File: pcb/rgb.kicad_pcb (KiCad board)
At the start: 2 copper layers, 58 x 48 mm, 59 parts, among them J1 2.54-2*8P, J3 B4PS-VH, J4 TYPE-C-31-M-12, J5 TF-01A, J7 B4PS-VH, U1 SY8286ARAC, U2 SY8286ARAC, U4 TACTILE, U5 ESP32-WROOM-32E, U7 CH340C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

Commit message: do we have space fo the RTC?
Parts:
- added BT1: CR2032, Battery:BatteryHolder_Multicomp_BC-2001_1x2032, B.Cu at (56.0, 98.0)
- added C30: 2u2, Capacitor_SMD:C_0603_1608Metric, F.Cu at (65.5, 118.5)
- added R12: 10k, Resistor_SMD:R_0603_1608Metric, F.Cu at (80.5, 113.5)
- added R14: 1k, Resistor_SMD:R_0603_1608Metric, F.Cu at (64.0, 102.5)
- added R16: 10k, Resistor_SMD:R_0603_1608Metric, F.Cu at (70.0, 77.0)
- added R17: 10k, Resistor_SMD:R_0603_1608Metric, F.Cu at (56.8, 105.0)
- added R18: 10k, Resistor_SMD:R_0603_1608Metric, F.Cu at (52.2, 105.0)
- added R19: 10k, Resistor_SMD:R_0603_1608Metric, F.Cu at (50.8, 105.0)
- added R20: 10k, Resistor_SMD:R_0603_1608Metric, F.Cu at (49.2, 105.0)
- added R21: 10k, Resistor_SMD:R_0603_1608Metric, F.Cu at (58.2, 105.0)
- added R22: 1k, Resistor_SMD:R_0603_1608Metric, F.Cu at (78.5, 99.5)
- added R23: 1k, Resistor_SMD:R_0603_1608Metric, F.Cu at (77.5, 97.0)
- added R24: 1k, Resistor_SMD:R_0603_1608Metric, F.Cu at (81.5, 99.5)
- added R25: 10k, Resistor_SMD:R_0603_1608Metric, F.Cu at (67.0, 112.5)
- added R26: 10k, Resistor_SMD:R_0603_1608Metric, F.Cu at (67.0, 114.0)
- added R4: 10k, Resistor_SMD:R_0603_1608Metric, F.Cu at (55.2, 105.0)
- added U3: DS3232M, Package_SO:SOIC-8_3.9x4.9mm_P1.27mm, F.Cu at (69.5, 118.5)
- D2: value GREEN -> GRN
- R10: value 56k -> 24k
- R13: value 22k -> 10k
- R6: value 10k -> 24k
- R7: value 22k -> 19k8
- U4: value TACTILE -> EVQQ2
- moved C6 4.93 mm to (74.0, 114.0), turned to 180 degrees
- moved J5 3.00 mm to (54.0, 113.5)
- moved C4 2.61 mm to (53.8, 105.0), turned to 90 degrees
- moved R14 0.25 mm to (65.5, 102.5)
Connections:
- J5 pad 1: unconnected-(J5-DAT2-Pad1) -> Net-(J5-DAT2)
- J5 pad 2: /SD_CS -> Net-(J5-DAT3/CD)
- J5 pad 3: /SD_MOSI -> /SD_CMD
- J5 pad 7: /SD_MISO -> /SD_D0
- J5 pad 8: unconnected-(J5-DAT1-Pad8) -> /SD_D1
- R9 pad 2: Net-(U5-IO33) -> Net-(U5-IO12)
- U5 pad 10: /SD_MISO -> /STB
- U5 pad 11: /SD_CLK -> /C
- U5 pad 12: /SD_MOSI -> /CLK
- U5 pad 13: /SD_CS -> /SD_CLK
- U5 pad 14: /OE -> Net-(U5-IO12)
- U5 pad 16: /CLK -> Net-(U5-IO13)
- U5 pad 23: /STB -> /SD_CMD
- U5 pad 24: /C -> /SD_D0
- U5 pad 25: Net-(U5-IO0) -> /esp_prog
- U5 pad 26: /D -> /SD_D1
- U5 pad 8: /E -> /D
- U5 pad 9: Net-(U5-IO33) -> /OE
- U7 pad 5: /USB_P -> /USB_P_S
- U7 pad 6: /USB_N -> /USB_N_S
- U9 pad 4: Net-(U9-DM) -> /USB_P_P
- U9 pad 5: Net-(U9-DM) -> /USB_N_P
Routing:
- net Net-(U5-IO33): track 35.3 -> 0.00 mm, vias 4 -> 0
- net /OE: track 35.3 -> 70.6 mm, vias 1 -> 5
- net /C: track 11.8 -> 38.0 mm, vias 1 -> 5
- net /SD_CS: track 24.9 -> 0.00 mm, vias 2 -> 0
- net /STB: track 18.5 -> 31.1 mm
- net /SD_MISO: track 12.7 -> 0.00 mm
- net /SD_CLK: track 26.2 -> 24.9 mm, vias 4 -> 2
- net GND: track 14.8 -> 13.5 mm, vias 81 -> 80
- net /RTC_SCL: track 0.00 -> 1.22 mm, vias 0 -> 1
- net Net-(U9-DM): track 1.00 -> 0.00 mm
- net (no net): track 0.00 -> 1.00 mm
- net /SD_MOSI: vias 4 -> 0
- net /CLK: vias 3 -> 7

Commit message: pcb: started to place components
looks like the Rev: 3 PCB will be the same size as Rev: 2
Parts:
- removed BT1: CR2032, Battery:BatteryHolder_Multicomp_BC-2001_1x2032
- removed C30: 2u2, Capacitor_SMD:C_0603_1608Metric
- removed R12, R13, R26: 10k, Resistor_SMD:R_0603_1608Metric
- removed the R14 at (65.5, 102.5)
- removed the R4 at (45.8, 89.5)
- removed U3: DS3232M, Package_SO:SOIC-8_3.9x4.9mm_P1.27mm
- added C31: 2u2, Capacitor_SMD:C_0603_1608Metric, F.Cu at (45.8, 89.0)
- added C32: 2u2, Capacitor_SMD:C_0603_1608Metric, F.Cu at (70.8, 118.2)
- added J6: V_BATT, Connector_PinHeader_2.54mm:PinHeader_1x02_P2.54mm_Vertical, F.Cu at (66.0, 118.0)
- added R27: 47k, Resistor_SMD:R_0603_1608Metric, F.Cu at (77.5, 103.5)
- added R28: 220k, Resistor_SMD:R_0603_1608Metric, F.Cu at (77.5, 101.8)
- added R53: 10k, Resistor_SMD:R_0603_1608Metric, F.Cu at (70.8, 113.8)
- added R54: 10k, Resistor_SMD:R_0603_1608Metric, F.Cu at (70.8, 112.0)
- added SW1: MS-22C01-G010, espirgbani:MS-22C01, F.Cu at (78.0, 109.5)
- added U11: RV-3028-C7, Package_SON:MicroCrystal_C7_SON-8_1.5x3.2mm_P0.9mm, F.Cu at (70.3, 120.8)
- R6: value 24k -> 47k
- moved R25 34.2 mm to (45.8, 85.7), turned to 90 degrees
- moved C6 3.58 mm to (70.8, 115.5), turned to 0 degrees
- moved C18 1.83 mm to (84.0, 108.2)
- moved C19 1.83 mm to (84.0, 111.0)
- moved R14 0.90 mm to (63.2, 102.0), turned to 180 degrees
- moved C20 0.75 mm to (82.2, 104.4)
- moved C21 0.75 mm to (82.2, 101.7)
- moved C23 0.25 mm to (87.5, 106.0)
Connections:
- R25 pad 1: /RTC_SCL -> /esp_reset
- U5 pad 5: unconnected-(U5-SENSOR_VN-Pad5) -> Net-(U5-SENSOR_VN)
- U5 pad 7: /pd_bad -> unconnected-(U5-IO35-Pad7)
- U9 pad 10: /pd_bad -> unconnected-(U9-PG-Pad10)
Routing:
- net /pd_bad: track 66.1 -> 0.00 mm, vias 4 -> 0
- net /OE: track 70.6 -> 35.2 mm, vias 5 -> 4
- net /SD_MOSI: track 33.5 -> 0.00 mm
- net /esp_reset: track 62.7 -> 31.9 mm
- net /USB_N_P: track 0.00 -> 25.5 mm, vias 0 -> 2
- net /C: track 38.0 -> 16.4 mm, vias 5 -> 3
- net /USB_P_P: track 0.00 -> 19.5 mm, vias 0 -> 2
- net /USB_N_S: track 0.00 -> 15.5 mm
- net /CLK: track 24.6 -> 39.7 mm, vias 7 -> 6
- net /STB: track 31.1 -> 18.5 mm
- net /USB_N: track 21.1 -> 33.0 mm
- net /SD_CLK: track 24.9 -> 13.5 mm, vias 2 -> 1
- net /USB_P_S: track 0.00 -> 9.87 mm
- net +3.3V: track 125.8 -> 116.6 mm
- net /USB_P: track 20.7 -> 27.9 mm
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
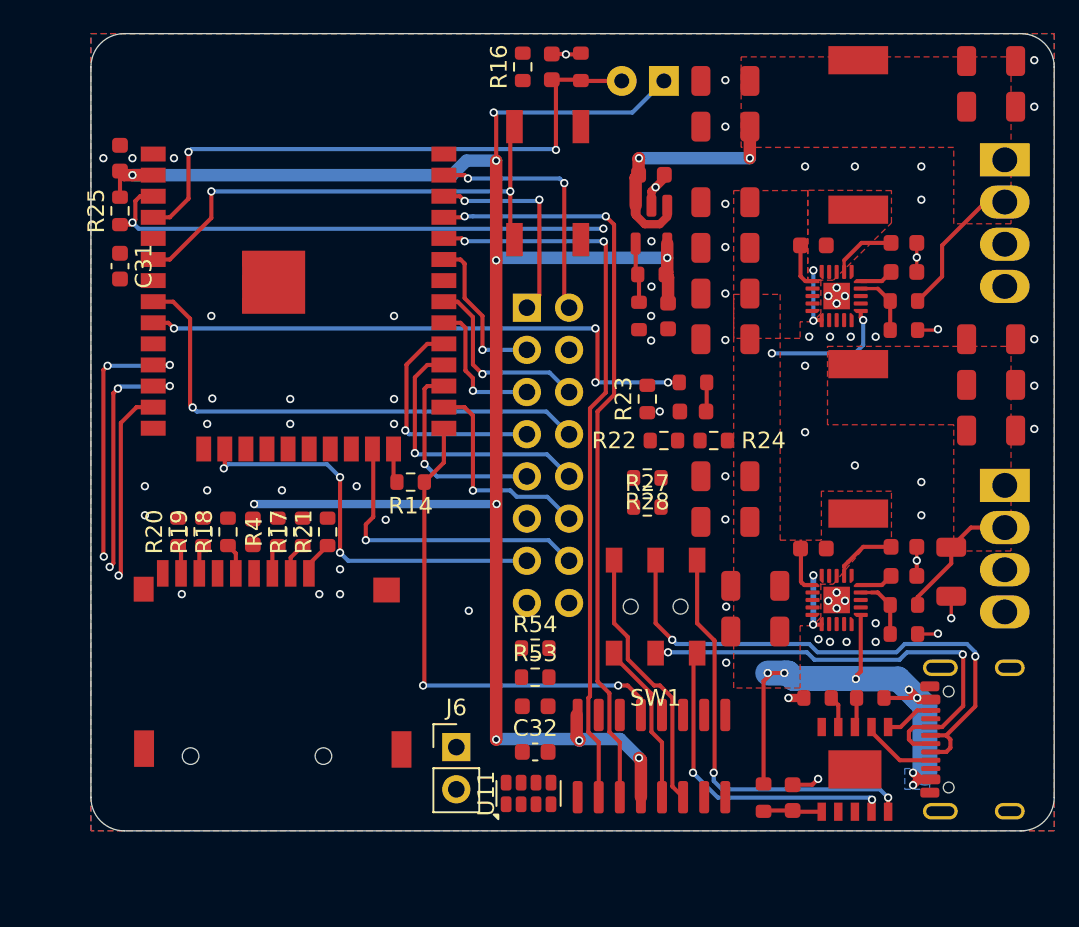
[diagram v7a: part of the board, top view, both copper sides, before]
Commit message: rev3 routing complete
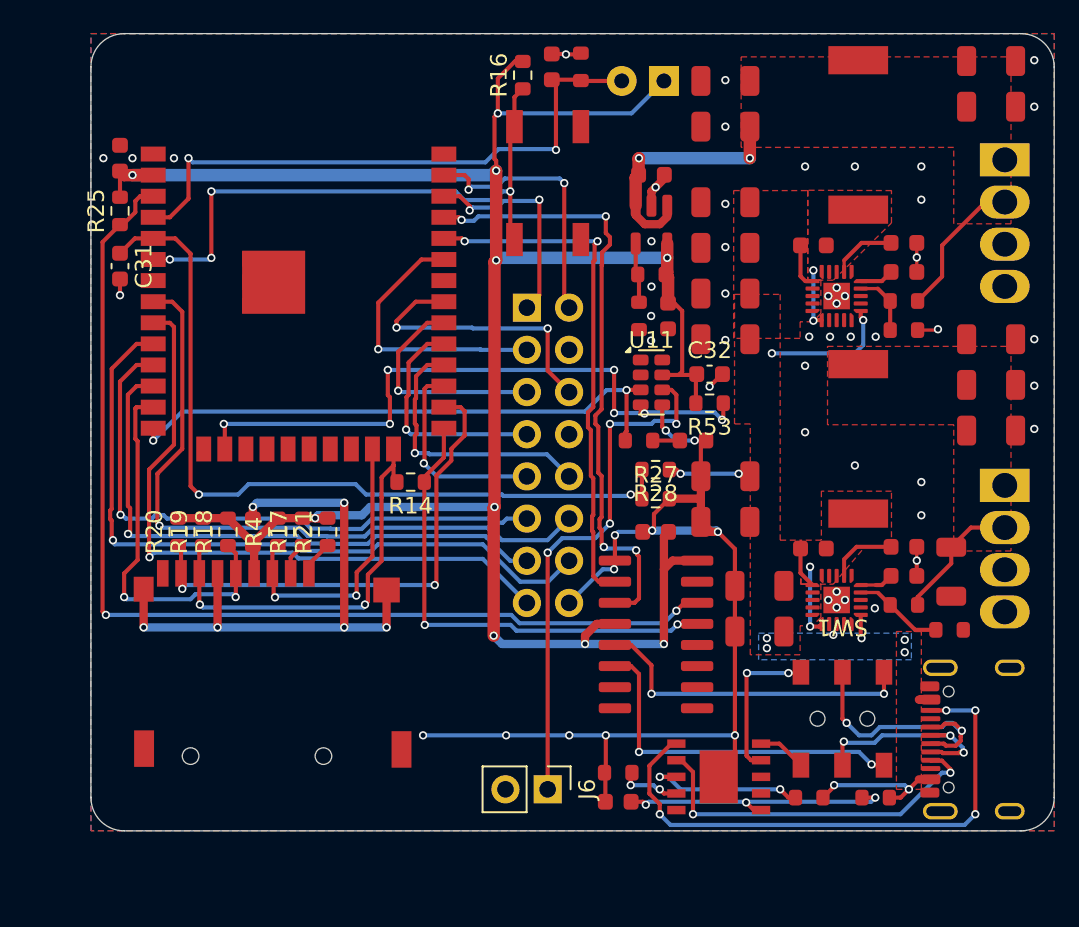
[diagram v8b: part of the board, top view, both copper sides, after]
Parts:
- removed R22, R23, R24: 1k, Resistor_SMD:R_0603_1608Metric
- removed R54: 10k, Resistor_SMD:R_0603_1608Metric
- moved U11 25.8 mm to (77.8, 96.0), turned to 0 degrees
- moved C32 25.1 mm to (81.2, 95.5)
- moved R53 19.6 mm to (81.2, 97.2), turned to 180 degrees
- moved SW1 13.1 mm to (89.2, 116.2), turned to 180 degrees
- moved R10 12.8 mm to (75.8, 119.5)
- moved C6 12.8 mm to (78.0, 105.0)
- moved C9 10.5 mm to (75.8, 121.2), turned to 180 degrees
- moved U9 8.21 mm to (81.8, 119.8), turned to 180 degrees
- moved U7 7.33 mm to (78.0, 111.2), turned to 0 degrees
- moved R11 7.04 mm to (87.2, 121.0)
- moved R8 6.75 mm to (91.2, 121.0), turned to 0 degrees
- moved J6 6.06 mm to (71.5, 120.5), turned to -90 degrees
- moved R9 4.78 mm to (77.0, 99.5)
- moved R15 2.76 mm to (95.7, 110.9)
- moved D2 1.75 mm to (80.2, 99.5), turned to 180 degrees
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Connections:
- R9 pad 2: Net-(U5-IO12) -> /RTC_SCL
- U5 pad 14: Net-(U5-IO12) -> /RTC_SCL
- U5 pad 16: Net-(U5-IO13) -> /RTC_SDA
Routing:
- net GND: track 14.0 -> 112.9 mm, vias 77 -> 65
- net Net-(U5-SENSOR_VN): track 0.00 -> 48.8 mm, vias 0 -> 2
- net /RTC_SDA: track 0.00 -> 39.6 mm, vias 0 -> 7
- net /RTC_SCL: track 0.00 -> 34.4 mm, vias 0 -> 2
- net Net-(J6-Pin_1): track 0.00 -> 31.6 mm, vias 0 -> 4
- net /esp_reset: track 31.9 -> 63.4 mm
- net /E: track 31.4 -> 0.00 mm, vias 1 -> 0
- net /CC2: track 2.98 -> 33.8 mm, vias 0 -> 4
- net /SD_D1: track 1.75 -> 30.6 mm, vias 0 -> 2
- net /D: track 13.0 -> 41.6 mm
- net /STB: track 18.5 -> 43.0 mm
- net +3.3V: track 116.6 -> 141.1 mm
- net /USB_N_P: track 25.5 -> 2.94 mm, vias 2 -> 0
- net /SD_D0: track 3.84 -> 25.0 mm, vias 0 -> 2
- net /USB_N: track 33.0 -> 13.1 mm, vias 2 -> 3
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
